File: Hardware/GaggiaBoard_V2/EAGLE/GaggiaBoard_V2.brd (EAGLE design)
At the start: 102 x 92 mm, 115 parts, among them IC1 LD117AS33TR, IC2 LD117AS33TR, J11 PIN262409-1, J12 PIN262409-1, J13 PIN262409-1, J14 PIN262409-1, J15 PIN262409-1, J16 PIN262409-1, J17 PIN262409-1, J18 PIN262409-1, J19 PIN262409-1, J2 Vertical Qwiic Connector, J20 PIN262409-1, J24 5033981892, J3 Vertical Qwiic Connector, J5 2PIN, J6 3PIN, J7 3PIN, J8 5PIN, J9 3PIN, K1 RELAY-SPDT-JZC-11F, K2 RELAY-SPDT-JZC-11F, K3 RELAY-SPDT-JZC-11F, Q1 600mA/40V, Q10 600mA/40V, Q2 600mA/40V, Q3 600mA/40V, Q4 600mA/40V, Q5 600mA/40V, Q6 600mA/40V, Q8 600mA/40V, Q9 600mA/40V, U1 BLACKPILL, U2 MAX31855K, U5 TXS0102

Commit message: part list fix
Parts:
- moved C8 8.56 mm to (92.0, 25.5), turned to 0 degrees
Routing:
- net 5V: track 344.2 -> 347.0 mm
- net AC_N: track 205.5 -> 207.3 mm
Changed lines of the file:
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@@
 <drawing>
 <settings>
-<setting alwaysvectorfont="yes"/>
+<setting alwaysvectorfont="no"/>
 <setting verticaltext="up"/>
 </settings>
@@
 </layers>
 <board>
-<fusionsync huburn="a.YnVzaW5lc3M6Z21haWwyMjIzNTY5" projecturn="a.YnVzaW5lc3M6Z21haWwyMjIzNTY5I0QyMDIyMDEwNDQ4MTQ5MTcwNg" f3durn="urn:adsk.wipprod:dm.lineage:6w6Byw4bTdmTaueqAgbUEw" pcbguid="" lastpulledtime="" lastsyncedchangeguid="" latestrevisionid="172b21af-06b0-469f-97ae-7bcfc94109dc" lastsyncedrevisionid="172b21af-06b0-469f-97ae-7bcfc94109dc" lastboardhashguid="f24e53fc-158b-1f6d-4315-241966646160" lastpushedtime="2022-07-08T06:02:15Z" linktopcb3d="true"/>
+<fusionsync huburn="a.YnVzaW5lc3M6Z21haWwyMjIzNTY5" projecturn="a.YnVzaW5lc3M6Z21haWwyMjIzNTY5I0QyMDIyMDEwNDQ4MTQ5MTcwNg" f3durn="urn:adsk.wipprod:dm.lineage:6w6Byw4bTdmTaueqAgbUEw" pcbguid="" lastpulledtime="" lastsyncedchangeguid="" latestrevisionid="f5b72319-5f83-45ac-8c5c-21c1cc47dbd0" lastsyncedrevisionid="f5b72319-5f83-45ac-8c5c-21c1cc47dbd0" lastboardhashguid="f5f3250e-0ac0-ee41-2de5-6bbe57c72a9f" lastpushedtime="2022-08-14T00:36:34Z" linktopcb3d="true"/>
 <plain>
 <wire x1="-2.5" y1="-6" x2="92.5" y2="-6" width="0" layer="20"/>
@@
 <attribute name="VALUE" x="66.095" y="7.635" size="1.27" layer="27" rot="R270"/>
 </element>
-<element name="C8" library="rcl" library_urn="urn:adsk.eagle:library:334" package="C0603" package3d_urn="urn:adsk.eagle:package:23616/2" value="10uF/16V" x="93" y="34" smashed="yes" rot="R90">
-<attribute name="LCSC" value="C86275" x="235.24" y="116.55" size="1.778" layer="27" rot="R90" display="off"/>
-<attribute name="NAME" x="91.965" y="33.365" size="0.6096" layer="25" rot="R90"/>
-<attribute name="POPULARITY" value="37" x="235.24" y="116.55" size="1.778" layer="27" rot="R90" display="off"/>
-<attribute name="SPICEPREFIX" value="C" x="235.24" y="116.55" size="1.778" layer="27" rot="R90" display="off"/>
-<attribute name="VALUE" x="94.905" y="33.365" size="1.27" layer="27" rot="R90"/>
+<element name="C8" library="rcl" library_urn="urn:adsk.eagle:library:334" package="C0603" package3d_urn="urn:adsk.eagle:package:23616/2" value="10uF/16V" x="92" y="25.5" smashed="yes">
+<attribute name="LCSC" value="C86275" x="174.55" y="-116.74" size="1.778" layer="27" display="off"/>
+<attribute name="NAME" x="89.206" y="25.138" size="0.6096" layer="25"/>
+<attribute name="POPULARITY" value="37" x="174.55" y="-116.74" size="1.778" layer="27" display="off"/>
+<attribute name="SPICEPREFIX" value="C" x="174.55" y="-116.74" size="1.778" layer="27" display="off"/>
+<attribute name="VALUE" x="91.365" y="23.595" size="1.27" layer="27"/>
 </element>
 <element name="C9" library="rcl" library_urn="urn:adsk.eagle:library:334" package="C0603" package3d_urn="urn:adsk.eagle:package:23616/2" value="10uF/16V" x="34" y="52" smashed="yes" rot="R90">
@@
 </element>
 <element name="IC1" library="v-reg" library_urn="urn:adsk.eagle:library:409" package="SOT223" package3d_urn="urn:adsk.eagle:package:30370/1" override_package3d_urn="urn:adsk.eagle:package:36461295/2" override_package_urn="urn:adsk.eagle:footprint:30315/1" value="LD117AS33TR" x="90" y="37" smashed="yes" rot="MR180">
-<attribute name="LCSC" value="C152529" x="209.38" y="125.9" size="1.778" layer="28" rot="MR180" display="off"/>
+<attribute name="LCSC" value="C26537" x="209.38" y="125.9" size="1.778" layer="28" rot="MR180" display="off"/>
 <attribute name="NAME" x="88.66" y="43.1492" size="1.27" layer="26" rot="MR180"/>
 <attribute name="POPULARITY" value="9" x="209.38" y="125.9" size="1.778" layer="28" rot="MR180" display="off"/>
@@
 </element>
 <element name="IC2" library="v-reg" library_urn="urn:adsk.eagle:library:409" package="SOT223" package3d_urn="urn:adsk.eagle:package:30370/1" override_package3d_urn="urn:adsk.eagle:package:36461293/2" override_package_urn="urn:adsk.eagle:footprint:30315/1" value="LD117AS33TR" x="39" y="54" smashed="yes" rot="R180">
-<attribute name="LCSC" value="C152529" x="16.14" y="163.22" size="1.778" layer="27" rot="R180" display="off"/>
+<attribute name="LCSC" value="C26537" x="16.14" y="163.22" size="1.778" layer="27" rot="R180" display="off"/>
 <attribute name="NAME" x="40.44" y="49.4492" size="1.27" layer="25" rot="R180"/>
 <attribute name="POPULARITY" value="9" x="16.14" y="163.22" size="1.778" layer="27" rot="R180" display="off"/>
@@
 </element>
 <element name="LED1" library="adafruit" library_urn="urn:adsk.eagle:library:420" package="CHIPLED_1206" package3d_urn="urn:adsk.eagle:package:6240560/1" override_package3d_urn="urn:adsk.eagle:package:36462256/4" override_package_urn="urn:adsk.eagle:footprint:6239914/1" value="" x="36" y="31" smashed="yes">
-<attribute name="LCSC" value="C375534" x="163" y="-96" size="1.778" layer="27" display="off"/>
+<attribute name="LCSC" value="C125086" x="163" y="-96" size="1.778" layer="27" display="off"/>
 <attribute name="NAME" x="37.73" y="29.93" size="0.6096" layer="25" rot="R90"/>
 <attribute name="VALUE" x="38.54" y="29.73" size="1.27" layer="27" rot="R90"/>
 </element>
 <element name="LED2" library="adafruit" library_urn="urn:adsk.eagle:library:420" package="CHIPLED_1206" package3d_urn="urn:adsk.eagle:package:6240560/1" override_package3d_urn="urn:adsk.eagle:package:36462272/2" override_package_urn="urn:adsk.eagle:footprint:6239914/1" value="" x="36" y="20" smashed="yes">
-<attribute name="LCSC" value="C375534" x="49.97" y="-115.89" size="1.778" layer="27" display="off"/>
+<attribute name="LCSC" value="C125086" x="49.97" y="-115.89" size="1.778" layer="27" display="off"/>
 <attribute name="NAME" x="37.73" y="18.93" size="0.6096" layer="25" rot="R90"/>
 <attribute name="VALUE" x="38.54" y="18.73" size="1.27" layer="27" rot="R90"/>
 </element>
 <element name="LED3" library="adafruit" library_urn="urn:adsk.eagle:library:420" package="CHIPLED_1206" package3d_urn="urn:adsk.eagle:package:6240560/1" override_package3d_urn="urn:adsk.eagle:package:36462279/2" override_package_urn="urn:adsk.eagle:footprint:6239914/1" value="" x="36" y="42" smashed="yes">
-<attribute name="LCSC" value="C375534" x="55.05" y="-93.89" size="1.778" layer="27" display="off"/>
+<attribute name="LCSC" value="C125086" x="55.05" y="-93.89" size="1.778" layer="27" display="off"/>
 <attribute name="NAME" x="37.83" y="41.03" size="0.6096" layer="25" rot="R90"/>
 <attribute name="VALUE" x="38.54" y="40.73" size="1.27" layer="27" rot="R90"/>
@@
 <element name="U1" library="discrete" library_urn="urn:adsk.eagle:library:211" package="BLACKPILL" override_package3d_urn="urn:adsk.eagle:package:36462313/2" override_package_urn="urn:adsk.eagle:footprint:36462314/1" value="BLACKPILL" x="70" y="38" smashed="yes" rot="R180">
 <attribute name="NAME" x="44.4" y="51.3" size="1.27" layer="21" rot="R180"/>
-<attribute name="VALUE" x="95.342" y="26.224" size="1.27" layer="21" rot="R180"/>
+<attribute name="VALUE" x="95.088" y="28.002" size="1.016" layer="21" rot="R180"/>
 </element>
 <element name="U2" library="SparkFun-IC-Conversion" package="SO08" override_package3d_urn="urn:adsk.eagle:package:36462208/2" override_package_urn="urn:adsk.eagle:footprint:36462209/1" value="MAX31855K" x="82" y="69" smashed="yes" rot="R180">
@@
 <wire x1="92.3" y1="37.737" x2="92.3" y2="40.15" width="1.27" layer="16"/>
 <contactref element="C8" pad="1"/>
-<wire x1="93" y1="33.15" x2="93" y2="30.52" width="0.8128" layer="1"/>
-<wire x1="93" y1="30.52" x2="92.86" y2="30.38" width="0.8128" layer="1"/>
+<wire x1="92.86" y1="30.38" x2="91.15" y2="28.67" width="0.8128" layer="1"/>
+<wire x1="91.15" y1="28.67" x2="91.15" y2="25.5" width="0.8128" layer="1"/>
 </signal>
 <signal name="3V3">
@@
 <wire x1="41" y1="5" x2="41" y2="6.422" width="0.4064" layer="1"/>
 <wire x1="41" y1="6.422" x2="41.578" y2="7" width="0.4064" layer="1"/>
-<wire x1="41" y1="5" x2="41" y2="-1.672" width="0.4064" layer="16"/>
+<wire x1="41" y1="5" x2="42.27" y2="3.73" width="0.4064" layer="16"/>
+<wire x1="42.27" y1="3.73" x2="42.27" y2="-1.672" width="0.4064" layer="16"/>
 <wire x1="5" y1="-1.19" x2="5" y2="0.35" width="0.4064" layer="16"/>
-<wire x1="41" y1="-1.672" x2="39.37" y2="-3.302" width="0.4064" layer="16"/>
-<wire x1="39.37" y1="-3.302" x2="7.112" y2="-3.302" width="0.4064" layer="16"/>
+<wire x1="42.27" y1="-1.672" x2="40.64" y2="-3.302" width="0.4064" layer="16"/>
+<wire x1="40.64" y1="-3.302" x2="7.112" y2="-3.302" width="0.4064" layer="16"/>
 <wire x1="7.112" y1="-3.302" x2="5" y2="-1.19" width="0.4064" layer="16"/>
 <polygon width="0.254" layer="16">
@@
 <contactref element="D5" pad="A"/>
 <contactref element="C6" pad="2"/>
-<wire x1="58" y1="6.20289375" x2="58" y2="8.05" width="0.4064" layer="1"/>
-<wire x1="59.2056" y1="4.99729375" x2="58" y2="6.20289375" width="0.4064" layer="1"/>
-<wire x1="57" y1="0.15" x2="59.2056" y2="2.3556" width="0.4064" layer="1"/>
-<wire x1="59.2056" y1="2.3556" x2="59.2056" y2="4.99729375" width="0.4064" layer="1"/>
+<wire x1="58" y1="6.58389375" x2="58" y2="8.05" width="0.4064" layer="1"/>
+<wire x1="59.3326" y1="5.25129375" x2="58" y2="6.58389375" width="0.4064" layer="1"/>
+<wire x1="57" y1="0.15" x2="59.3326" y2="2.4826" width="0.4064" layer="1"/>
+<wire x1="59.3326" y1="2.4826" x2="59.3326" y2="5.25129375" width="0.4064" layer="1"/>
 <wire x1="56" y1="8.95" x2="57.1" y2="8.95" width="0.4064" layer="1"/>
 <wire x1="57.1" y1="8.95" x2="58" y2="8.05" width="0.4064" layer="1"/>
@@
 <wire x1="10" y1="5.65" x2="10" y2="0.35" width="2.54" layer="1"/>
 <wire x1="10" y1="0.35" x2="10.65" y2="1" width="2.54" layer="1"/>
-<wire x1="10.65" y1="1" x2="14.57" y2="1" width="2.54" layer="1"/>
+<wire x1="10.65" y1="1" x2="14.57" y2="1" width="3.81" layer="1"/>
 <wire x1="10" y1="5.65" x2="10" y2="0.35" width="2.54" layer="16"/>
 <wire x1="10" y1="0.35" x2="10.65" y2="1" width="2.54" layer="16"/>
-<wire x1="10.65" y1="1" x2="14.57" y2="1" width="2.54" layer="16"/>
+<wire x1="10.65" y1="1" x2="14.57" y2="1" width="3.81" layer="16"/>
 </signal>
 </signals>

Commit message: V2.1 update
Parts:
- removed IC2: LD117AS33TR, v-reg:SOT223
- removed J24: 5033981892, discrete:503398-1892_MOL
- removed Q7: (no value), microbuilder:SOT363
- removed R16, R17, R18, R19: 10K, rcl:R0603
- removed SJ1, SJ2: (no value), microbuilder:SOLDERJUMPER_ARROW_NOPASTE
- moved IC1 53.8 mm to (39.0, 54.0), flipped to the top
- moved J1 8.00 mm to (93.0, 5.00), turned to 90 degrees
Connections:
- removed net UART2_5V_RX: J1.2, Q7.3, R16.1, SJ2.2
- removed net UART2_5V_TX: J1.3, Q7.6, R17.1, SJ1.2
- net 3V3: no longer IC2.4, J24.4, Q7.2, Q7.5, R18.2, R19.2
- net 5V: no longer IC2.3, R16.2, R17.2
- net GND: no longer IC2.1, J24.6
- net SPI1_MISO: no longer J24.7
- net SPI1_MOSI: no longer J24.3
- net SPI1_NSS: no longer J24.2
- net SPI1_SCK: no longer J24.5
- net UART2_RX: now also J1.2; no longer Q7.4, R18.1, SJ2.1
- net UART2_TX: now also J1.3; no longer Q7.1, R19.1, SJ1.1
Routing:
- net SPI1_NSS: track 46.4 -> 0.00 mm, vias 1 -> 0
- net SPI1_MOSI: track 42.7 -> 0.00 mm, vias 1 -> 0
- net 3V3: track 250.0 -> 217.0 mm, vias 3 -> 2
- net UART2_5V_RX: track 25.6 -> 0.00 mm, vias 1 -> 0
- net UART2_5V_TX: track 8.37 -> 0.00 mm, vias 1 -> 0
- net 5V: track 347.0 -> 339.7 mm
- net UART2_RX: track 49.3 -> 51.0 mm, vias 4 -> 2
- net SPI1_MISO: track 35.9 -> 34.6 mm
- net SPI1_SCK: track 52.5 -> 51.3 mm
- net GND: track 99.2 -> 98.0 mm
- net UART2_TX: track 48.9 -> 48.2 mm, vias 4 -> 2
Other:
- board text added: "iuiuiu v2.1"
- board text removed: "iuiuiu v2"

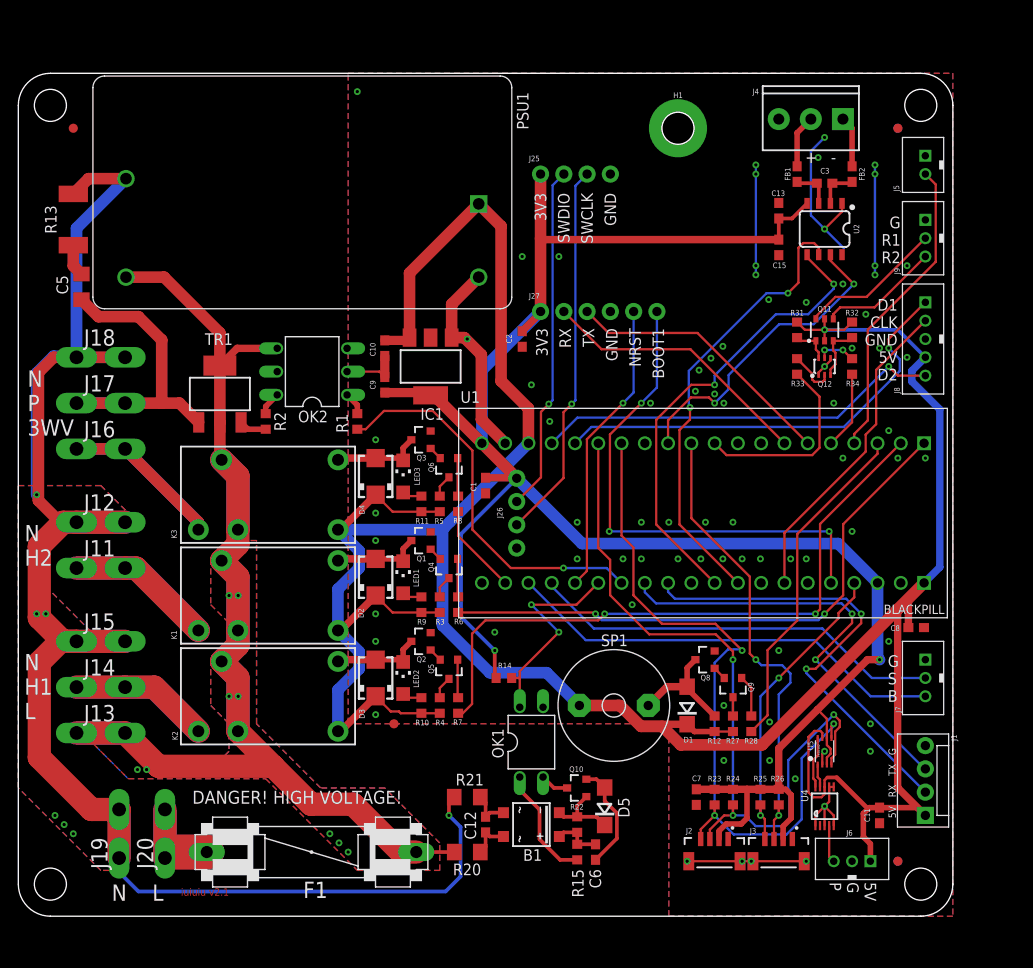
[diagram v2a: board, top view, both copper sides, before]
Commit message: Centroid added to Gerber
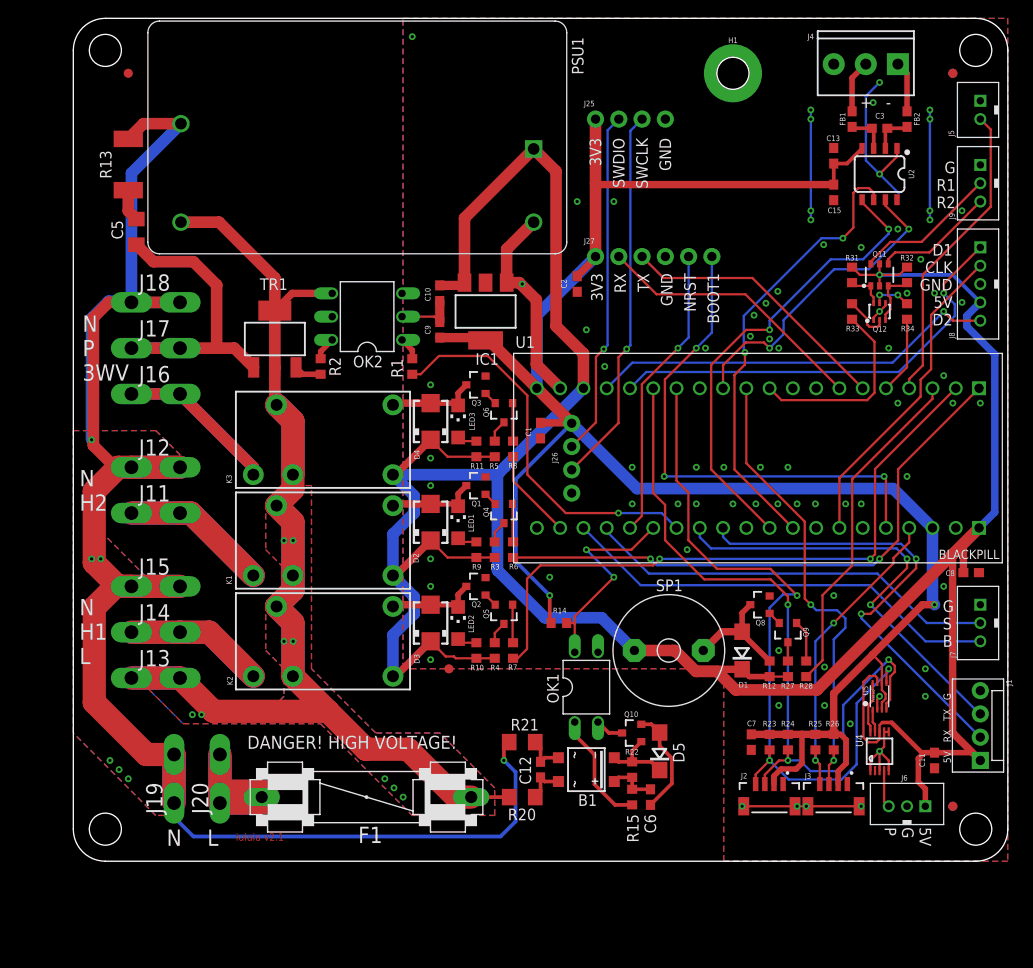
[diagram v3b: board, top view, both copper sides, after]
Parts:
- moved B1 8.49 mm to (56.0, 10.0)
- moved C1 8.49 mm to (51.0, 47.0)
- moved C10 8.49 mm to (40.0, 62.0)
- moved C11 8.49 mm to (94.0, 11.0)
- moved C12 8.49 mm to (51.0, 10.0)
- moved C13 8.49 mm to (83.0, 77.0)
- moved C15 8.49 mm to (83.0, 73.0)
- moved C2 8.49 mm to (55.0, 63.0)
- moved C3 8.49 mm to (88.0, 80.0)
- moved C5 8.49 mm to (6.89, 68.7)
- moved C6 8.49 mm to (63.0, 7.00)
- moved C7 8.49 mm to (74.0, 13.0)
- moved C8 8.49 mm to (98.0, 31.5)
- moved C9 8.49 mm to (40.0, 58.0)
- moved D1 8.49 mm to (73.0, 23.0)
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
